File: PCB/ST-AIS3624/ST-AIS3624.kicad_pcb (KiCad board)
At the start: 2 copper layers, 4 parts, among them J1 Conn_02x03_Odd_Even

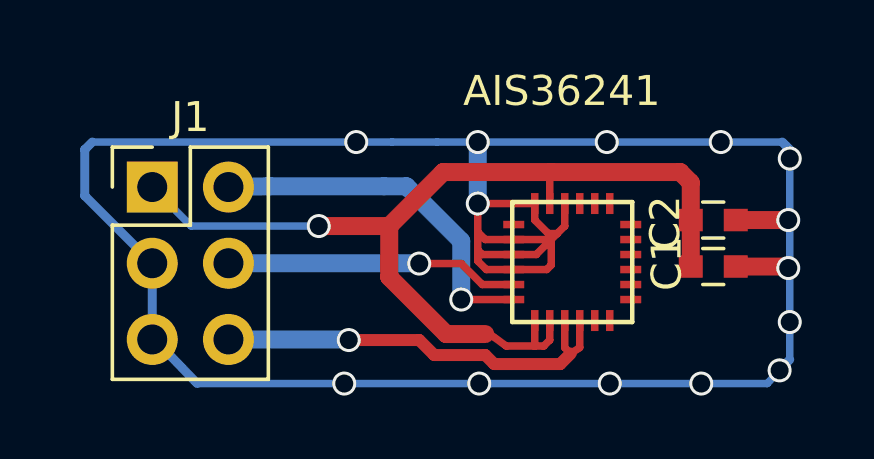
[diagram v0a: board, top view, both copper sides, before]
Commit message: PCB - ST-AIS v 1.5, ready to print
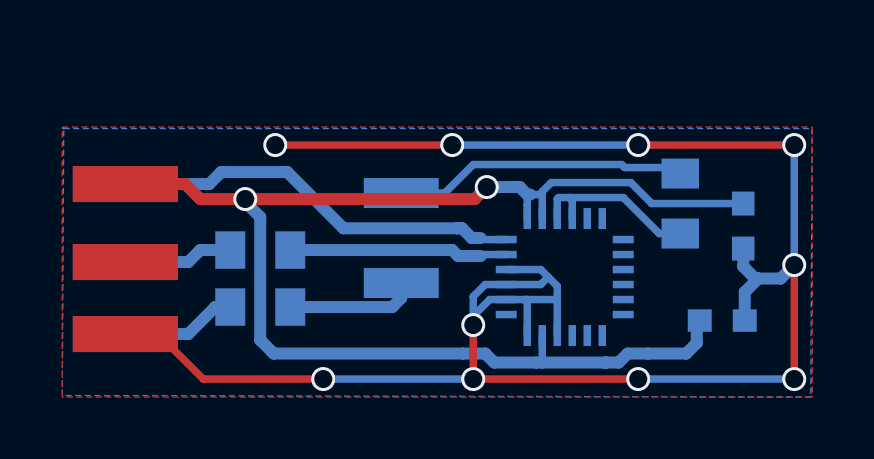
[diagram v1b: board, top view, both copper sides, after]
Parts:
- added J2, J6: Conn_01x01, DIY_KICAD_FOOTPRINT_LIBRARY:pastilles_CMS_rect_1,2_3,5, F.Cu at (124.1, 79.9)
- added J3, J5: Conn_01x01, DIY_KICAD_FOOTPRINT_LIBRARY:pastilles_CMS_rect_1,2_3,5, F.Cu at (124.1, 77.5)
- added J4: Conn_01x01, DIY_KICAD_FOOTPRINT_LIBRARY:pastilles_CMS_rect_1,2_3,5, F.Cu at (124.1, 74.9)
- added JP1: Jumper, Capacitors_SMD:C_1210, B.Cu at (133.3, 76.7)
- added JP2: Jumper, Capacitors_SMD:C_0805, B.Cu at (128.6, 77.1)
- added JP3: Jumper, Capacitors_SMD:C_0805, B.Cu at (128.6, 79.0)
- added JP4: Jumper, Capacitors_SMD:C_0805, B.Cu at (142.6, 75.5)
- AIS36241, C1, C2: moved to B.Cu
- J1: value Conn_02x03_Odd_Even -> Conn_01x01; footprint Pin_Headers:Pin_Header_Straight_2x03_Pitch2.54mm -> DIY_KICAD_FOOTPRINT_LIBRARY:pastilles_CMS_rect_1,2_3,5
- moved C1 1.82 mm to (144.0, 79.5)
- moved C2 1.02 mm to (144.7, 76.3), turned to 270 degrees
- moved J1 0.91 mm to (124.1, 74.9)
- moved AIS36241 0.56 mm to (138.8, 78.0), turned to 90 degrees
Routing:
- net GNDREF: track 81.3 -> 66.2 mm, vias 14 -> 10
- net /VDD: track 32.8 -> 45.1 mm, vias 1 -> 2
- net Net-(JP1-Pad1): track 0.00 -> 10.1 mm
- net /Miso/Mosi: track 14.2 -> 6.01 mm, vias 1 -> 0
- net Net-(JP1-Pad2): track 0.00 -> 4.32 mm
- net Net-(J6-Pad1): track 0.00 -> 4.01 mm
- net Net-(J5-Pad1): track 0.00 -> 3.81 mm
- net /SCLK: track 9.80 -> 7.30 mm, vias 1 -> 0
- net /CS/SCL: track 12.3 -> 13.7 mm, vias 1 -> 0
- added copper zone on B.Cu, net GNDREF
- added copper zone on F.Cu, net GNDREF

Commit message: PCB - AIS3624 update after review with meca staff
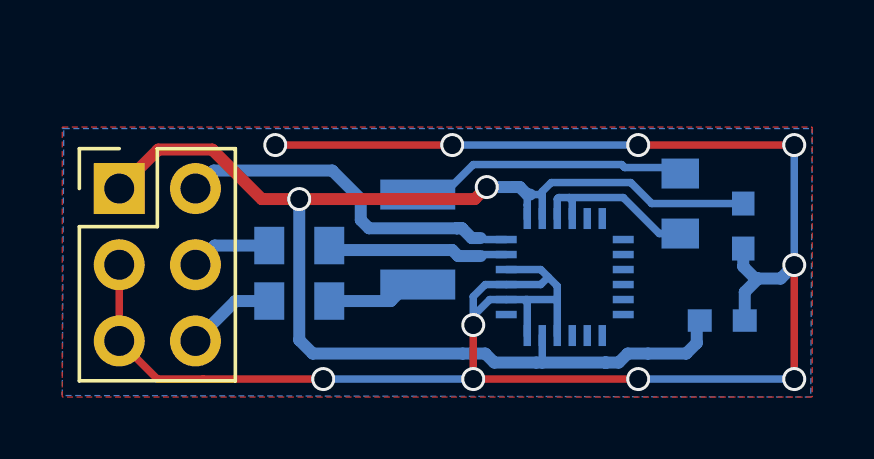
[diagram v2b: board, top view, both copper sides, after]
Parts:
- removed J2, J3, J4, J5, J6: Conn_01x01, DIY_KICAD_FOOTPRINT_LIBRARY:pastilles_CMS_rect_1,2_3,5
- J1: value Conn_01x01 -> Conn_02x03_Odd_Even; footprint DIY_KICAD_FOOTPRINT_LIBRARY:pastilles_CMS_rect_1,2_3,5 -> Pin_Headers:Pin_Header_Straight_2x03_Pitch2.54mm
- moved JP3 1.32 mm to (129.9, 78.8)
- moved JP2 1.31 mm to (129.9, 77.0)
- moved JP1 0.55 mm to (133.8, 76.8)
- moved J1 0.25 mm to (123.9, 75.0)
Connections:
- JP2 pad 1: Net-(J5-Pad1) -> Net-(J1-Pad4)
- JP3 pad 2: Net-(J6-Pad1) -> Net-(J1-Pad6)
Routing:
- net Net-(J6-Pad1): track 4.01 -> 0.00 mm
- net Net-(J5-Pad1): track 3.81 -> 0.00 mm
- net Net-(J1-Pad6): track 0.00 -> 3.01 mm
- net Net-(J1-Pad4): track 0.00 -> 2.73 mm
- net GNDREF: track 66.2 -> 68.8 mm
- net /CS/SCL: track 13.7 -> 11.8 mm
- net /SCLK: track 7.30 -> 6.07 mm
- net Net-(JP1-Pad2): track 4.32 -> 3.18 mm
- net Net-(JP1-Pad1): track 10.1 -> 9.57 mm

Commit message: Docs - AIS3624 add archive controle pcb & minor update
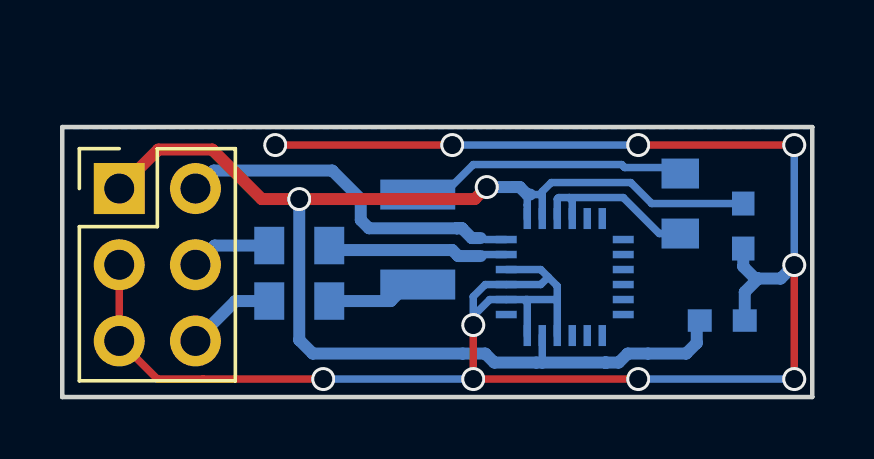
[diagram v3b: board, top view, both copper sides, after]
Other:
- board outline added: 25 x 9 mm
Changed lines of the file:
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@@
     (links 21)
     (no_connects 0)
-    (area 107.214287 61.8 150.785715 90.850001)
+    (area 107.214287 61.8 147.400002 85.725)
     (thickness 1.6)
-    (drawings 7)
+    (drawings 26)
     (tracks 134)
     (zones 0)
@@
     (visible_elements 7FFFF77F)
     (pcbplotparams
-      (layerselection 0x00000_80000001)
+      (layerselection 0x000c4_80000001)
       (usegerberextensions false)
       (excludeedgelayer true)
@@
     )
   )
-  (dimension 8 (width 0.3) (layer F.Fab)
-    (gr_text "8,000 mm" (at 145 89.5) (layer F.Fab)
-      (effects (font (size 1.5 1.5) (thickness 0.3)))
-    )
-    (feature1 (pts (xy 139 83.75) (xy 139 88.45)))
-    (feature2 (pts (xy 147 83.75) (xy 147 88.45)))
-    (crossbar (pts (xy 147 85.75) (xy 139 85.75)))
-    (arrow1a (pts (xy 139 85.75) (xy 140.126504 85.163579)))
-    (arrow1b (pts (xy 139 85.75) (xy 140.126504 86.336421)))
-    (arrow2a (pts (xy 147 85.75) (xy 145.873496 85.163579)))
-    (arrow2b (pts (xy 147 85.75) (xy 145.873496 86.336421)))
-  )
+  (gr_line (start 122 82) (end 122 73) (angle 90) (layer B.Mask) (width 0.2))
+  (gr_line (start 147 82) (end 122 82) (angle 90) (layer B.Mask) (width 0.2))
+  (gr_line (start 147 73) (end 147 82) (angle 90) (layer B.Mask) (width 0.2))
+  (gr_line (start 122 73) (end 147 73) (angle 90) (layer B.Mask) (width 0.2))
+  (gr_line (start 122 82) (end 122 73) (angle 90) (layer B.Paste) (width 0.2))
+  (gr_line (start 147 82) (end 122 82) (angle 90) (layer B.Paste) (width 0.2))
+  (gr_line (start 147 73) (end 147 82) (angle 90) (layer B.Paste) (width 0.2))
+  (gr_line (start 122 73) (end 147 73) (angle 90) (layer B.Paste) (width 0.2))
+  (gr_line (start 122 82) (end 122 73) (angle 90) (layer F.Mask) (width 0.2))
+  (gr_line (start 147 82) (end 122 82) (angle 90) (layer F.Mask) (width 0.2))
+  (gr_line (start 147 73) (end 147 82) (angle 90) (layer F.Mask) (width 0.2))
+  (gr_line (start 122 73) (end 147 73) (angle 90) (layer F.Mask) (width 0.2))
+  (gr_line (start 122 82) (end 122 73) (angle 90) (layer B.Paste) (width 0.2))
+  (gr_line (start 147 82) (end 122 82) (angle 90) (layer B.Paste) (width 0.2))
+  (gr_line (start 147 73) (end 147 82) (angle 90) (layer B.Paste) (width 0.2))
+  (gr_line (start 122 73) (end 147 73) (angle 90) (layer B.Paste) (width 0.2))
+  (gr_line (start 122 82) (end 122 73) (angle 90) (layer Edge.Cuts) (width 0.15))
+  (gr_line (start 147 82) (end 122 82) (angle 90) (layer Edge.Cuts) (width 0.15))
+  (gr_line (start 147 73) (end 147 82) (angle 90) (layer Edge.Cuts) (width 0.15))
+  (gr_line (start 122 73) (end 147 73) (angle 90) (layer Edge.Cuts) (width 0.15))
   (gr_line (start 147 73) (end 122 73) (angle 90) (layer F.Fab) (width 0.2))
   (gr_line (start 147 82) (end 147 73) (angle 90) (layer F.Fab) (width 0.2))
@@
   (via (at 129.1 73.6) (size 0.8) (drill 0.6) (layers F.Cu B.Cu) (net 4))
   (segment (start 129.9 75.4) (end 128.65 75.4) (width 0.4) (layer F.Cu) (net 5))
-  (segment (start 125.2 73.75) (end 123.9 75.05) (width 0.4) (layer F.Cu) (net 5) (status 800000))
+  (segment (start 125.2 73.75) (end 123.9 75.05) (width 0.4) (layer F.Cu) (net 5))
   (segment (start 127 73.75) (end 125.2 73.75) (width 0.4) (layer F.Cu) (net 5))
   (segment (start 128.65 75.4) (end 127 73.75) (width 0.4) (layer F.Cu) (net 5))
@@
   (segment (start 132.95 78.8) (end 133.5 78.25) (width 0.4) (layer B.Cu) (net 18))
   (segment (start 133.5 78.25) (end 133.85 78.25) (width 0.4) (layer B.Cu) (net 18))
-  (segment (start 133.85 75.25) (end 134.7 75.25) (width 0.25) (layer B.Cu) (net 19) (status C00000))
-  (segment (start 134.7 75.25) (end 135.7 74.25) (width 0.25) (layer B.Cu) (net 19) (status 400000))
+  (segment (start 133.85 75.25) (end 134.7 75.25) (width 0.25) (layer B.Cu) (net 19))
+  (segment (start 134.7 75.25) (end 135.7 74.25) (width 0.25) (layer B.Cu) (net 19))
   (segment (start 140.750002 74.35) (end 142.4 74.35) (width 0.25) (layer B.Cu) (net 19))
   (segment (start 140.650002 74.25) (end 140.750002 74.35) (width 0.25) (layer B.Cu) (net 19))

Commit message: PCB-AIS3624 v2.0 verified
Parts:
- removed JP1: Jumper, Capacitors_SMD:C_1210
- removed JP3, JP4: Jumper, Capacitors_SMD:C_0805
- AIS36241: value AIS3624DQTR -> Acc1; moved to F.Cu
- C1, C2, JP2: moved to F.Cu
- moved C1 9.54 mm to (134.6, 77.8), turned to 180 degrees
- moved AIS36241 1.38 mm to (140.1, 77.7), turned to 180 degrees
- moved C2 1.14 mm to (144.4, 77.4)
- moved JP2 0.58 mm to (129.6, 76.5), turned to 90 degrees
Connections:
- J1 pad 6: Net-(J1-Pad6) -> /Miso/Mosi
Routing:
- net Net-(JP1-Pad1): track 9.57 -> 0.00 mm
- net /Miso/Mosi: track 6.01 -> 14.6 mm
- net GNDREF: track 68.8 -> 60.9 mm, vias 10 -> 11
- net /SCLK: track 6.07 -> 10.8 mm
- net Net-(JP1-Pad2): track 3.18 -> 0.00 mm
- net Net-(J1-Pad6): track 3.01 -> 0.00 mm
- net /CS/SCL: track 11.8 -> 13.5 mm
- net /VDD: track 44.8 -> 45.1 mm, vias 2 -> 0
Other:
- board text added: "AIS3624 Eval Board CHAMP - October/2018"
- board text added: "MOSI MISO"
- board text added: "SCL SCLK"
- board text added: "VDD"
